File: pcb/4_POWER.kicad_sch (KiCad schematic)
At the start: 53 parts, among them Q1 AO3407A, U10 HL2304, U5 AP74700QW6-7, U6 HL2304, U7 TPS54331DR, U8 TPS54331DR, U9 AP74700QW6-7

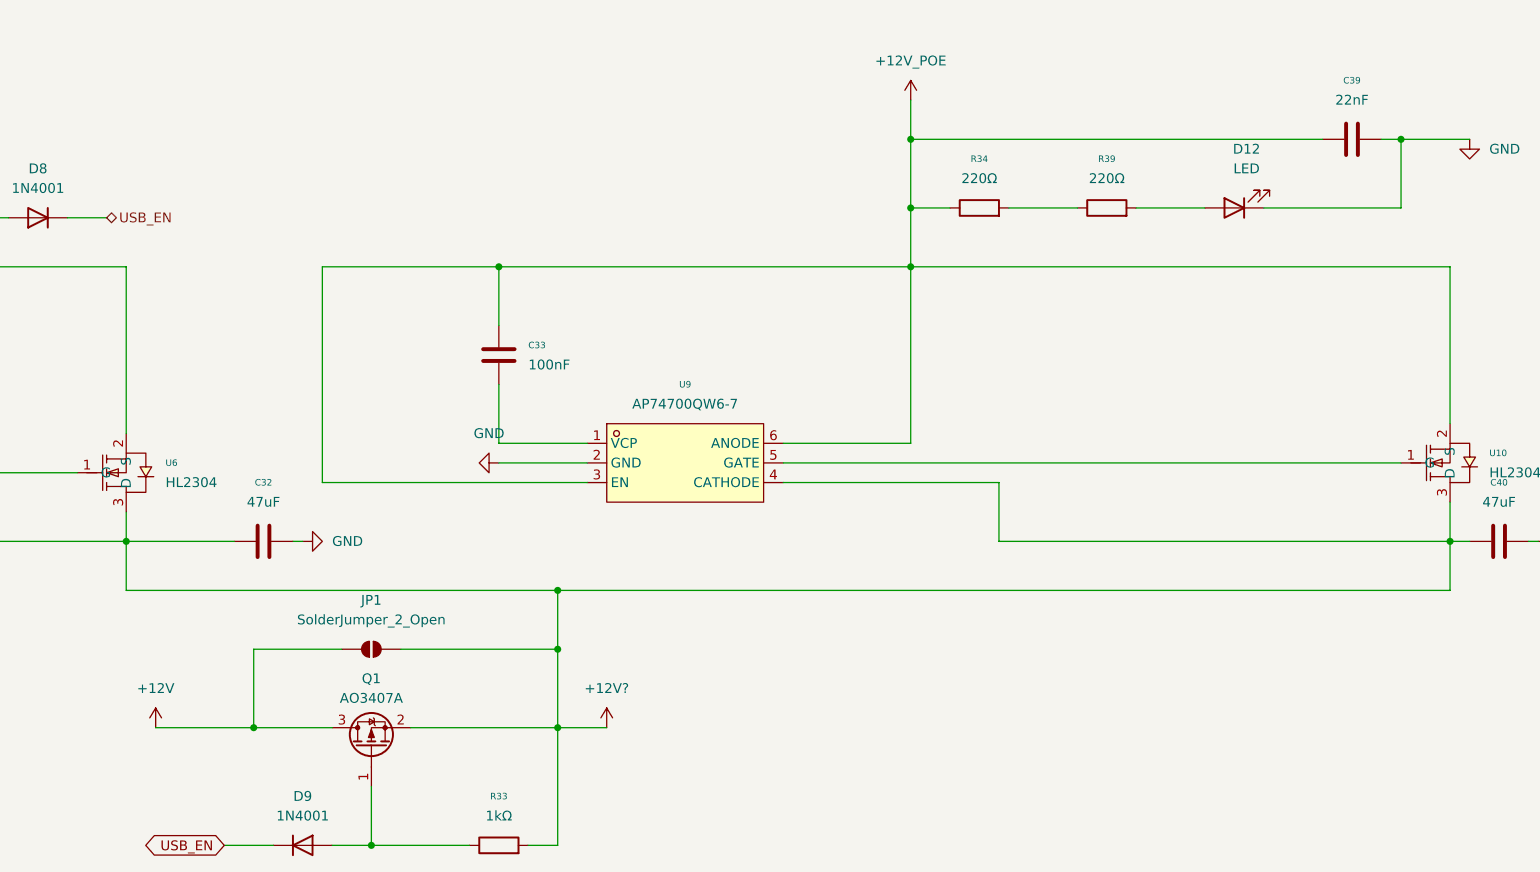
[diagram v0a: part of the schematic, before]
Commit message: 4 layer pcb
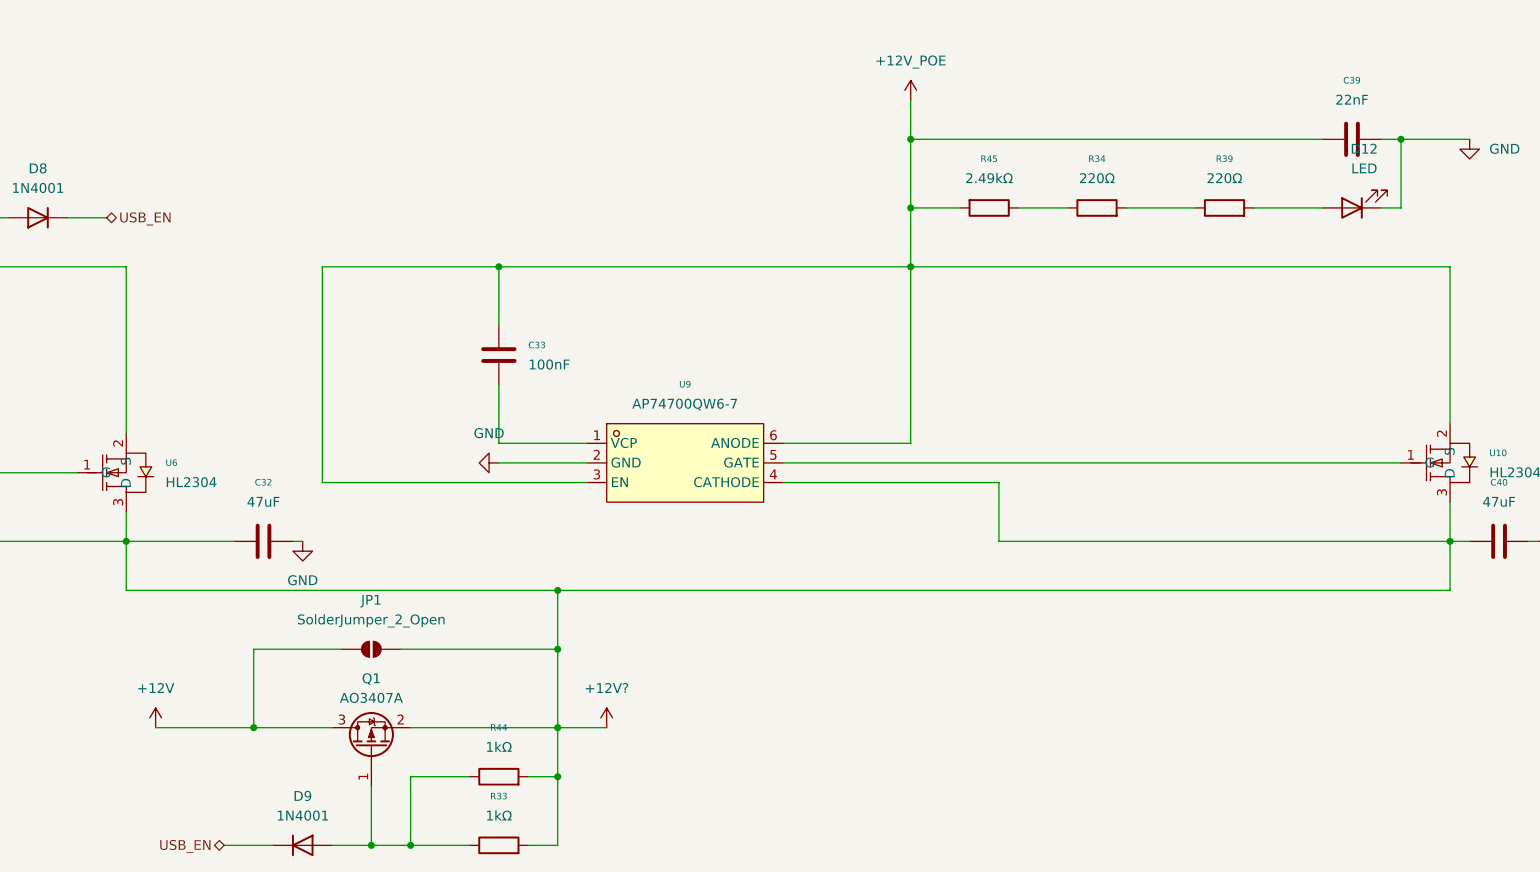
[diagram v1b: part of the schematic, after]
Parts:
- added R44: 1kΩ, Resistor_SMD:R_0603_1608Metric, symbol Device:R
- added R45: 2.49kΩ, Resistor_SMD:R_0603_1608Metric, symbol Device:R
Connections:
- net +12V?: now also R44.2
- net +12V_POE: now also R45.2; no longer R34.1
- net at D9.2 (A), Q1.1 (G), R33.1: now also R44.1
- new net: R34.1, R45.1
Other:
- moved on the sheet: D12, R34, R39

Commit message: review version
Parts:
- C32, C36, C37, C38, C40: footprint Capacitor_SMD:C_0805_2012Metric -> Capacitor_SMD:C_1206_3216Metric; LCSC C16780 -> C22367835
